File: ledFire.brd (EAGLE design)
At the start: 61 x 33 mm, 29 parts, among them Q1 MUN5235DW1T1G, Q2 MUN5235DW1T1G, U1 MCP1640, U2 ATtiny84A-SSU

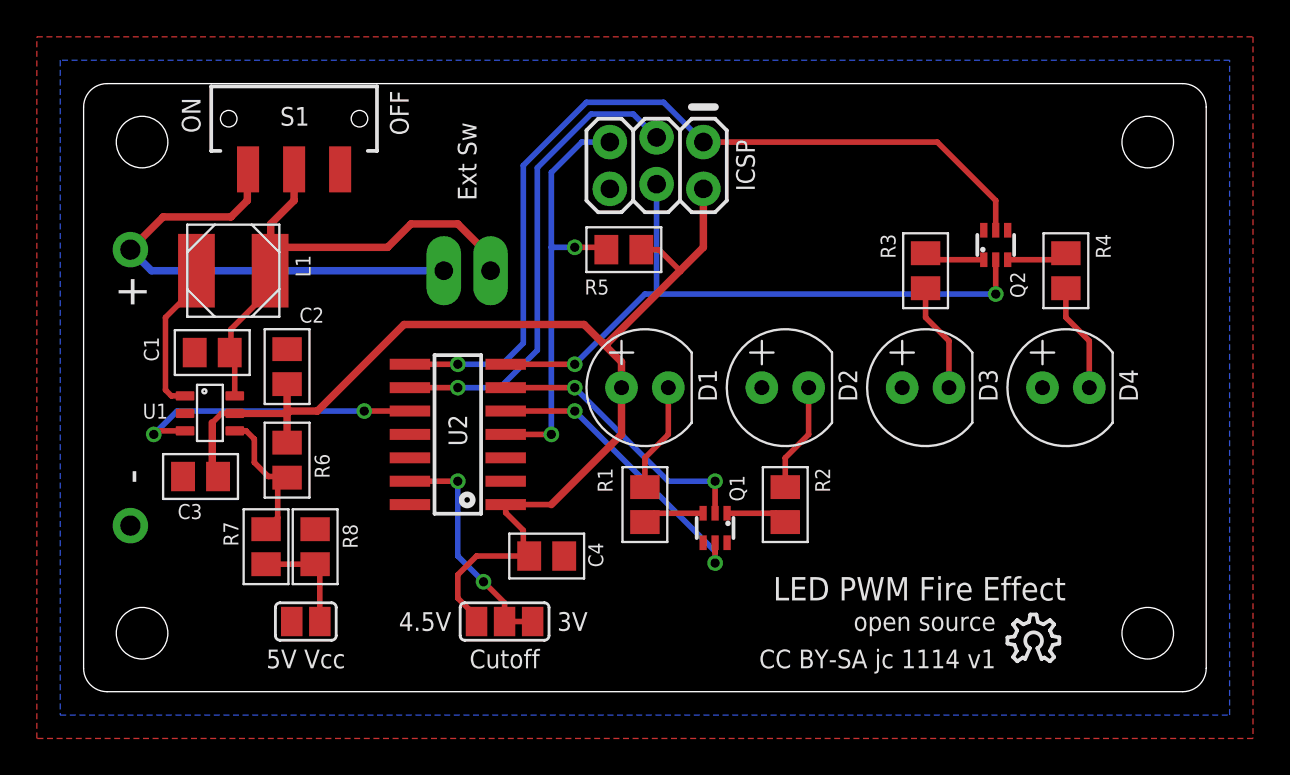
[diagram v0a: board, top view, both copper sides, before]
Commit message: v1.1, board corrections.
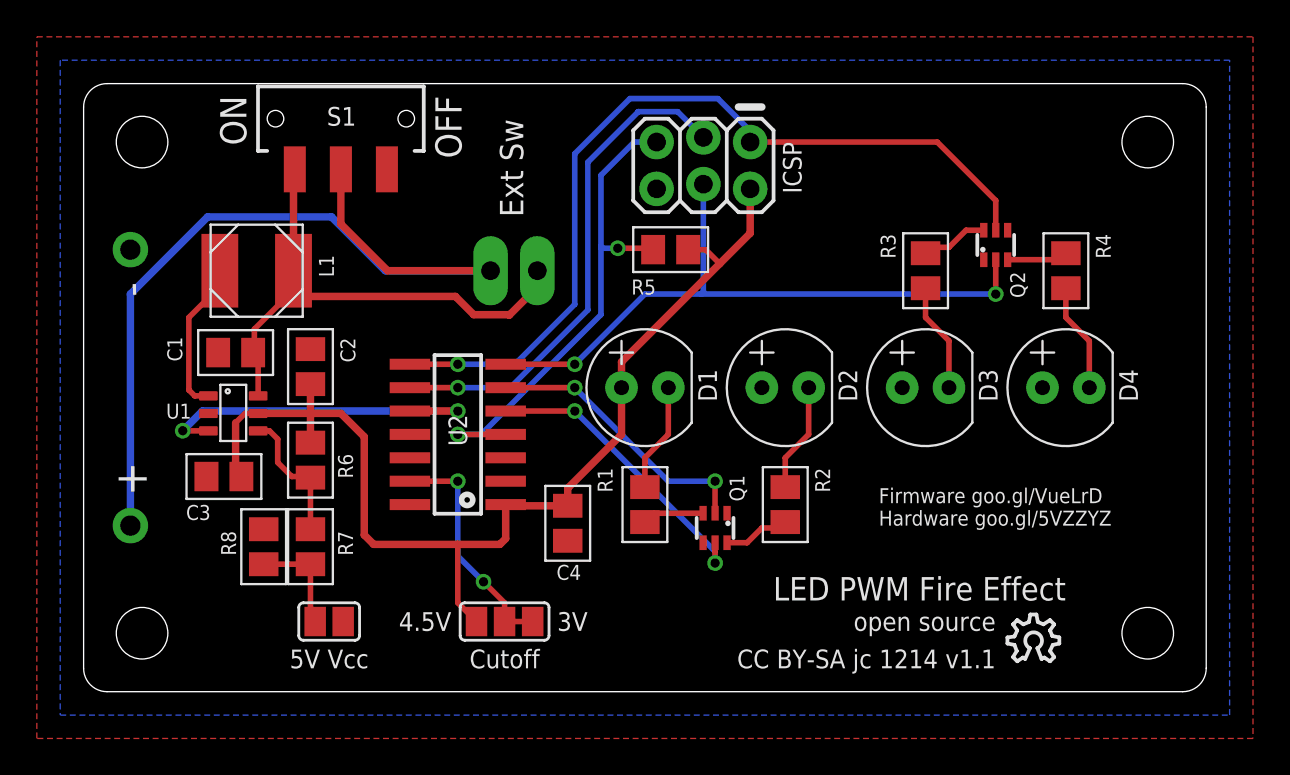
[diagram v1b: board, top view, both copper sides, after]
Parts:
- moved R8 2.79 mm to (9.78, 7.87)
- moved S1 2.54 mm to (14.0, 31.1)
- moved JP1 2.54 mm to (36.2, 29.8)
- moved JP2 2.54 mm to (22.1, 22.9)
- moved R5 2.54 mm to (31.9, 24.0)
- moved R7 2.41 mm to (12.3, 7.87)
- moved C4 2.11 mm to (26.3, 9.14), turned to 270 degrees
- moved C2 1.27 mm to (12.3, 17.7)
- moved R6 1.27 mm to (12.3, 12.6)
- moved SJ1 1.27 mm to (13.3, 3.81), turned to 180 degrees
- moved C1 1.27 mm to (8.26, 18.4)
- moved C3 1.27 mm to (7.62, 11.7)
- moved U1 1.27 mm to (8.13, 15.1)
- moved L1 1.27 mm to (9.40, 22.9)
- flipped B1 to the bottom, turned to 180 degrees
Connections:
- net GND: now also Q1.1, Q2.1; no longer Q1.6, Q2.6
- net N$10: now also S1.2; no longer S1.1
- net N$4: now also Q2.6; no longer Q2.1
- net N$8: now also Q1.6; no longer Q1.1
- net VIN: now also S1.1; no longer S1.2
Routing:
- net N$10: track 26.7 -> 47.2 mm
- net VCC: track 67.3 -> 60.5 mm
- net RESET: track 23.6 -> 27.3 mm
- net PA3: track 16.2 -> 19.4 mm
- net SCK/SCL: track 25.9 -> 27.4 mm
- net VIN: track 27.8 -> 28.7 mm
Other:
- board text added: "CC BY-SA jc 1214 v1.1"
- board text added: "Firmware goo.gl/VueLrD Hardware goo.gl/5VZZYZ"
- board text removed: "CC BY-SA jc 1114 v1"

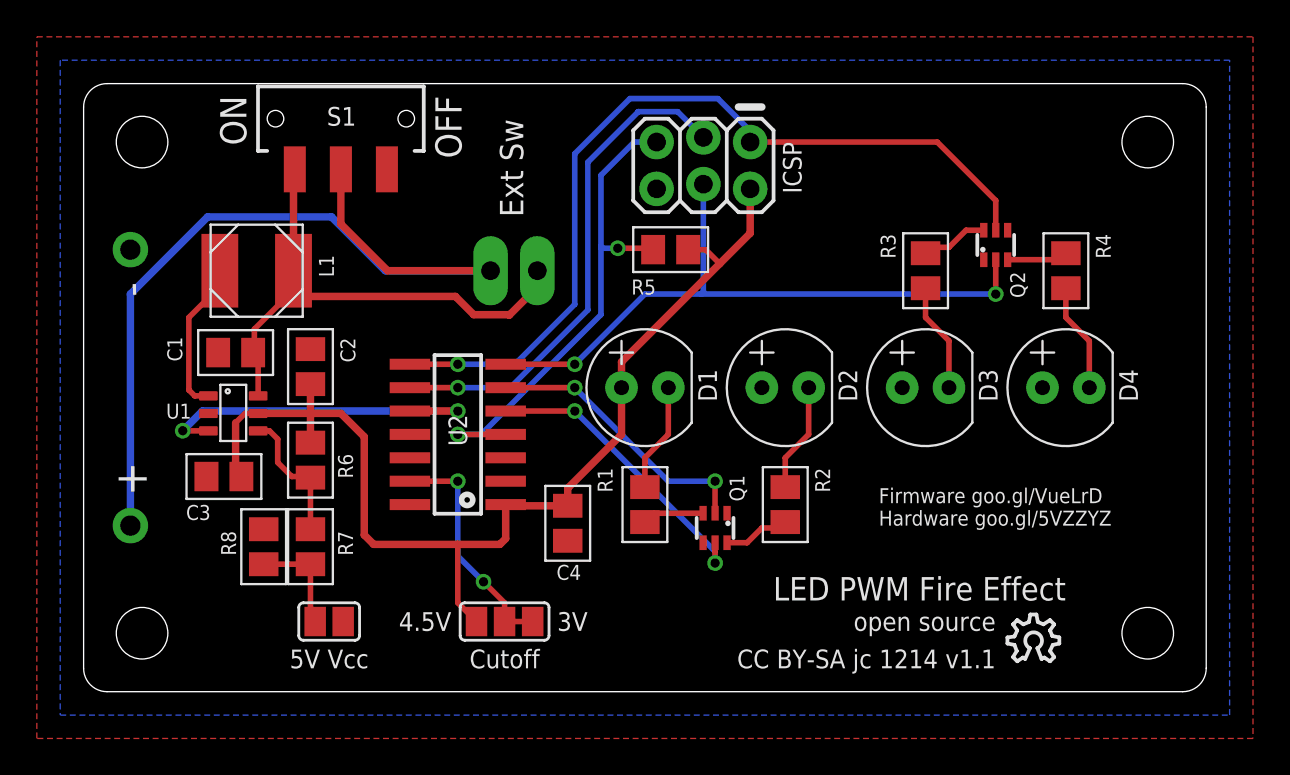
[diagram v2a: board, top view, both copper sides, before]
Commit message: Tweak SOT363 footprint.
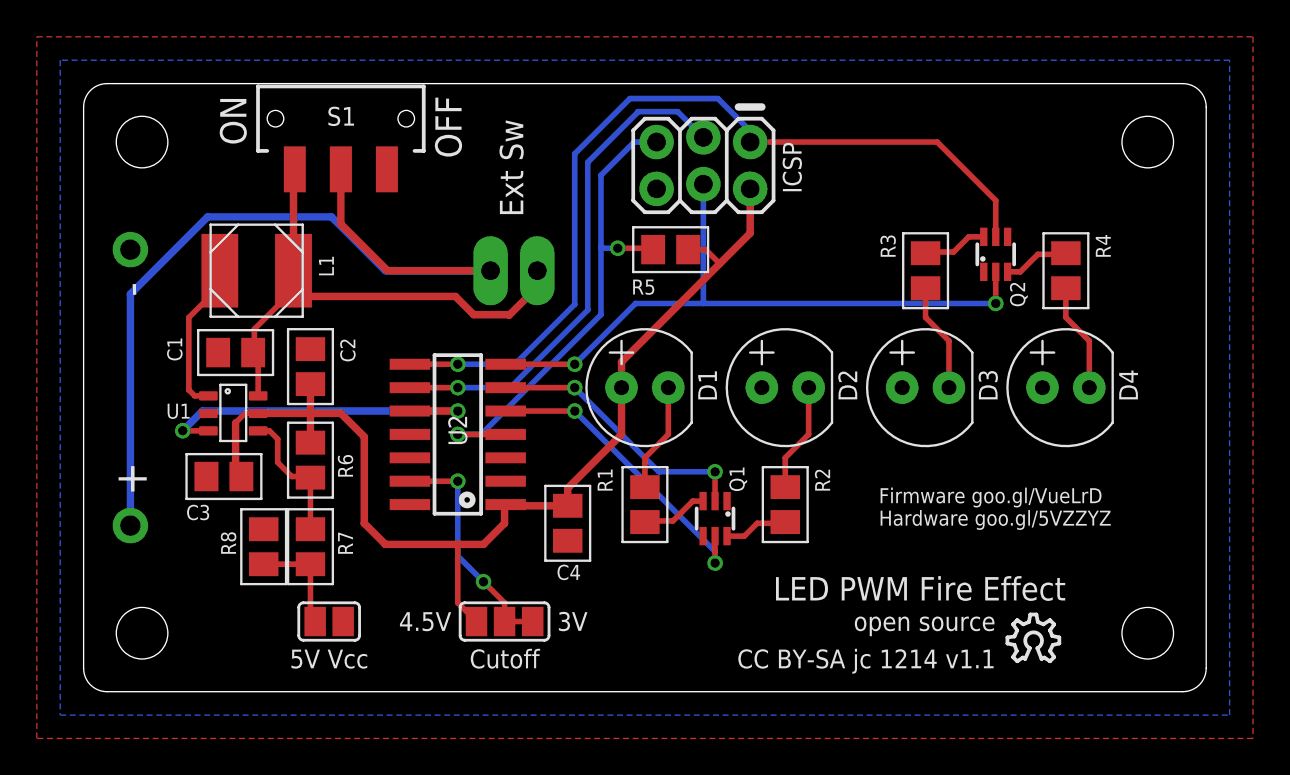
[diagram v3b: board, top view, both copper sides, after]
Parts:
- U1: value MCP1640 -> MCP1640D
- moved Q2 0.51 mm to (49.5, 23.7)
- moved Q1 0.51 mm to (34.3, 9.40)
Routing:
- net VCC: track 60.5 -> 59.6 mm
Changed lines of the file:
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@@
 <setting verticaltext="up"/>
 </settings>
-<grid distance="0.05" unitdist="inch" unit="inch" style="dots" multiple="1" display="yes" altdistance="0.002" altunitdist="inch" altunit="inch"/>
+<grid distance="0.05" unitdist="inch" unit="inch" style="dots" multiple="1" display="yes" altdistance="0.005" altunitdist="inch" altunit="inch"/>
 <layers>
 <layer number="1" name="Top" color="4" fill="1" visible="yes" active="yes"/>
@@
 </autorouter>
 <elements>
-<element name="U1" library="_jc" package="SOT23-6" value="MCP1640" x="8.128" y="15.113" smashed="yes" rot="R270">
+<element name="U1" library="_jc" package="SOT23-6" value="MCP1640D" x="8.128" y="15.113" smashed="yes" rot="R270">
 <attribute name="NAME" x="4.477" y="14.827" size="0.8128" layer="21" ratio="16"/>
 </element>
@@
 <attribute name="VALUE" x="23.789" y="10.644" size="0.8128" layer="27" ratio="16" rot="R270"/>
 </element>
-<element name="Q1" library="_jc" package="SOT363_PHILIPS" value="MUN5235DW1T1G" x="34.29" y="8.89" smashed="yes" rot="R180">
-<attribute name="NAME" x="35.888" y="10.33" size="0.8128" layer="25" ratio="16" rot="R90"/>
-<attribute name="VALUE" x="35.39" y="11.59" size="0.8128" layer="27" ratio="16" rot="R180"/>
-</element>
-<element name="Q2" library="_jc" package="SOT363_PHILIPS" value="MUN5235DW1T1G" x="49.53" y="24.257" smashed="yes">
-<attribute name="NAME" x="51.128" y="21.379" size="0.8128" layer="25" ratio="16" rot="R90"/>
-<attribute name="VALUE" x="48.43" y="21.557" size="0.8128" layer="27" ratio="16"/>
+<element name="Q1" library="_jc" package="SOT363_PHILIPS" value="MUN5235DW1T1G" x="34.29" y="9.398" smashed="yes" rot="R180">
+<attribute name="NAME" x="35.888" y="10.838" size="0.8128" layer="25" ratio="16" rot="R90"/>
+<attribute name="VALUE" x="35.39" y="12.098" size="0.8128" layer="27" ratio="16" rot="R180"/>
+</element>
+<element name="Q2" library="_jc" package="SOT363_PHILIPS" value="MUN5235DW1T1G" x="49.53" y="23.749" smashed="yes">
+<attribute name="NAME" x="51.128" y="20.871" size="0.8128" layer="25" ratio="16" rot="R90"/>
+<attribute name="VALUE" x="48.43" y="21.049" size="0.8128" layer="27" ratio="16"/>
 </element>
 <element name="D1" library="_jc" package="LED5MM" value="5mm" x="30.48" y="16.51" smashed="yes">
@@
 <wire x1="33.782" y1="24.003" x2="34.544" y2="23.241" width="0.3048" layer="1"/>
 <wire x1="13.97" y1="15.113" x2="15.24" y2="13.843" width="0.4064" layer="1"/>
-<wire x1="15.24" y1="13.843" x2="15.24" y2="8.509" width="0.4064" layer="1"/>
-<wire x1="15.24" y1="8.509" x2="15.748" y2="8.001" width="0.4064" layer="1"/>
-<wire x1="15.748" y1="8.001" x2="20.32" y2="8.001" width="0.4064" layer="1"/>
-<wire x1="20.32" y1="8.001" x2="22.606" y2="8.001" width="0.4064" layer="1"/>
-<wire x1="22.606" y1="8.001" x2="22.92" y2="8.315" width="0.4064" layer="1"/>
-<wire x1="22.92" y1="8.315" x2="22.92" y2="10.16" width="0.4064" layer="1"/>
 <wire x1="22.92" y1="10.16" x2="22.986" y2="10.094" width="0.4064" layer="1"/>
 <wire x1="22.986" y1="10.094" x2="26.289" y2="10.094" width="0.4064" layer="1"/>
@@
 <wire x1="26.289" y1="11.049" x2="29.21" y2="13.97" width="0.4064" layer="1"/>
 <wire x1="21.336" y1="3.81" x2="20.32" y2="4.826" width="0.3048" layer="1"/>
+<wire x1="15.24" y1="13.843" x2="15.24" y2="9.144" width="0.4064" layer="1"/>
+<wire x1="15.24" y1="9.144" x2="16.383" y2="8.001" width="0.4064" layer="1"/>
+<wire x1="16.383" y1="8.001" x2="20.32" y2="8.001" width="0.4064" layer="1"/>
+<wire x1="20.32" y1="8.001" x2="21.717" y2="8.001" width="0.4064" layer="1"/>
+<wire x1="21.717" y1="8.001" x2="22.86" y2="9.144" width="0.4064" layer="1"/>
+<wire x1="22.86" y1="9.144" x2="22.86" y2="10.1" width="0.4064" layer="1"/>
+<wire x1="22.86" y1="10.1" x2="22.92" y2="10.16" width="0.4064" layer="1"/>
 <wire x1="20.32" y1="4.826" x2="20.32" y2="8.001" width="0.3048" layer="1"/>
 </signal>
@@
 <wire x1="36.195" y1="29.845" x2="46.355" y2="29.845" width="0.3048" layer="1"/>
 <wire x1="46.355" y1="29.845" x2="49.53" y2="26.67" width="0.3048" layer="1"/>
-<wire x1="49.53" y1="26.67" x2="49.53" y2="25.057" width="0.3048" layer="1"/>
+<wire x1="49.53" y1="26.67" x2="49.53" y2="24.699" width="0.3048" layer="1"/>
 <wire x1="36.195" y1="30.099" x2="36.195" y2="29.845" width="0.3048" layer="16"/>
 <wire x1="23.4188" y1="17.78" x2="20.32" y2="17.78" width="0.3048" layer="16"/>
@@
 <via x="26.67" y="17.78" extent="1-16" drill="0.5"/>
 <wire x1="26.67" y1="17.78" x2="22.92" y2="17.78" width="0.3048" layer="1"/>
-<wire x1="49.53" y1="23.457" x2="49.53" y2="21.59" width="0.3048" layer="1"/>
-<via x="49.53" y="21.59" extent="1-16" drill="0.5"/>
-<wire x1="49.53" y1="21.59" x2="33.528" y2="21.59" width="0.3048" layer="16"/>
-<wire x1="33.528" y1="21.59" x2="30.48" y2="21.59" width="0.3048" layer="16"/>
-<wire x1="30.48" y1="21.59" x2="26.67" y2="17.78" width="0.3048" layer="16"/>
-<wire x1="33.655" y1="27.559" x2="33.655" y2="21.717" width="0.3048" layer="16"/>
-<wire x1="33.655" y1="21.717" x2="33.528" y2="21.59" width="0.3048" layer="16"/>
+<wire x1="49.53" y1="22.799" x2="49.53" y2="21.082" width="0.3048" layer="1"/>
+<via x="49.53" y="21.082" extent="1-16" drill="0.5"/>
+<wire x1="26.67" y1="17.78" x2="29.972" y2="21.082" width="0.3048" layer="16"/>
+<wire x1="29.972" y1="21.082" x2="33.655" y2="21.082" width="0.3048" layer="16"/>
+<wire x1="33.655" y1="21.082" x2="49.53" y2="21.082" width="0.3048" layer="16"/>
+<wire x1="33.655" y1="27.559" x2="33.655" y2="21.082" width="0.3048" layer="16"/>
 </signal>
 <signal name="PB2">
@@
 <wire x1="34.29" y1="7.62" x2="34.29" y2="6.985" width="0.3048" layer="16"/>
 <via x="34.29" y="6.985" extent="1-16" drill="0.5"/>
-<wire x1="34.29" y1="6.985" x2="34.29" y2="8.09" width="0.3048" layer="1"/>
+<wire x1="34.29" y1="6.985" x2="34.29" y2="8.448" width="0.3048" layer="1"/>
 </signal>
 <signal name="PA7">
@@
 <via x="26.67" y="16.51" extent="1-16" drill="0.5"/>
 <wire x1="26.67" y1="16.51" x2="22.92" y2="16.51" width="0.3048" layer="1"/>
-<wire x1="34.29" y1="9.69" x2="34.29" y2="11.43" width="0.3048" layer="1"/>
-<via x="34.29" y="11.43" extent="1-16" drill="0.5"/>
-<wire x1="26.67" y1="16.51" x2="31.75" y2="11.43" width="0.3048" layer="16"/>
-<wire x1="31.75" y1="11.43" x2="34.29" y2="11.43" width="0.3048" layer="16"/>
+<wire x1="34.29" y1="10.348" x2="34.29" y2="11.938" width="0.3048" layer="1"/>
+<via x="34.29" y="11.938" extent="1-16" drill="0.5"/>
+<wire x1="26.67" y1="16.51" x2="31.242" y2="11.938" width="0.3048" layer="16"/>
+<wire x1="31.242" y1="11.938" x2="34.29" y2="11.938" width="0.3048" layer="16"/>
 </signal>
 <signal name="N$1">
@@
 <contactref element="R1" pad="2"/>
 <contactref element="Q1" pad="3"/>
-<wire x1="33.64" y1="9.69" x2="30.96" y2="9.69" width="0.3048" layer="1"/>
-<wire x1="30.96" y1="9.69" x2="30.48" y2="9.21" width="0.3048" layer="1"/>
+<wire x1="33.64" y1="10.348" x2="33.081" y2="10.348" width="0.3048" layer="1"/>
+<wire x1="33.081" y1="10.348" x2="32.004" y2="9.271" width="0.3048" layer="1"/>
+<wire x1="32.004" y1="9.271" x2="30.541" y2="9.271" width="0.3048" layer="1"/>
+<wire x1="30.541" y1="9.271" x2="30.48" y2="9.21" width="0.3048" layer="1"/>
 </signal>
 <signal name="N$8">
 <contactref element="R2" pad="2"/>
 <contactref element="Q1" pad="6"/>
-<wire x1="34.94" y1="8.09" x2="36.03" y2="8.09" width="0.3048" layer="1"/>
-<wire x1="36.03" y1="8.09" x2="36.83" y2="8.89" width="0.3048" layer="1"/>
-<wire x1="36.83" y1="8.89" x2="37.78" y2="8.89" width="0.3048" layer="1"/>
-<wire x1="37.78" y1="8.89" x2="38.1" y2="9.21" width="0.3048" layer="1"/>
+<wire x1="34.94" y1="8.448" x2="35.88" y2="8.448" width="0.3048" layer="1"/>
+<wire x1="35.88" y1="8.448" x2="36.576" y2="9.144" width="0.3048" layer="1"/>
+<wire x1="36.576" y1="9.144" x2="38.034" y2="9.144" width="0.3048" layer="1"/>
+<wire x1="38.034" y1="9.144" x2="38.1" y2="9.21" width="0.3048" layer="1"/>
 </signal>
 <signal name="N$9">
 <contactref element="R4" pad="2"/>
 <contactref element="Q2" pad="3"/>
-<wire x1="50.18" y1="23.457" x2="52.987" y2="23.457" width="0.3048" layer="1"/>
-<wire x1="52.987" y1="23.457" x2="53.34" y2="23.81" width="0.3048" layer="1"/>
+<wire x1="50.18" y1="22.799" x2="50.866" y2="22.799" width="0.3048" layer="1"/>
+<wire x1="50.866" y1="22.799" x2="51.816" y2="23.749" width="0.3048" layer="1"/>
+<wire x1="51.816" y1="23.749" x2="53.279" y2="23.749" width="0.3048" layer="1"/>
+<wire x1="53.279" y1="23.749" x2="53.34" y2="23.81" width="0.3048" layer="1"/>
 </signal>
 <signal name="N$14">
@@
 <contactref element="R3" pad="2"/>
 <contactref element="Q2" pad="6"/>
-<wire x1="48.88" y1="25.057" x2="47.917" y2="25.057" width="0.3048" layer="1"/>
-<wire x1="47.917" y1="25.057" x2="46.99" y2="24.13" width="0.3048" layer="1"/>
-<wire x1="46.99" y1="24.13" x2="46.04" y2="24.13" width="0.3048" layer="1"/>
-<wire x1="46.04" y1="24.13" x2="45.72" y2="23.81" width="0.3048" layer="1"/>
+<wire x1="48.88" y1="24.699" x2="48.067" y2="24.699" width="0.3048" layer="1"/>
+<wire x1="48.067" y1="24.699" x2="47.244" y2="23.876" width="0.3048" layer="1"/>
+<wire x1="47.244" y1="23.876" x2="45.786" y2="23.876" width="0.3048" layer="1"/>
+<wire x1="45.786" y1="23.876" x2="45.72" y2="23.81" width="0.3048" layer="1"/>
 </signal>
 <signal name="N$10">
